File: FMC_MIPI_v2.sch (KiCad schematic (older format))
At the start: 0 parts

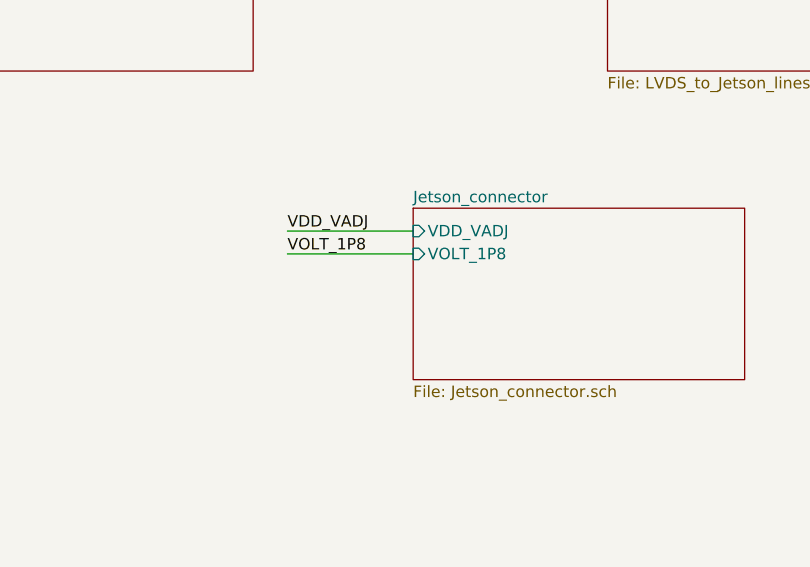
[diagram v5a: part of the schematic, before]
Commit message: added enable line for slow signals
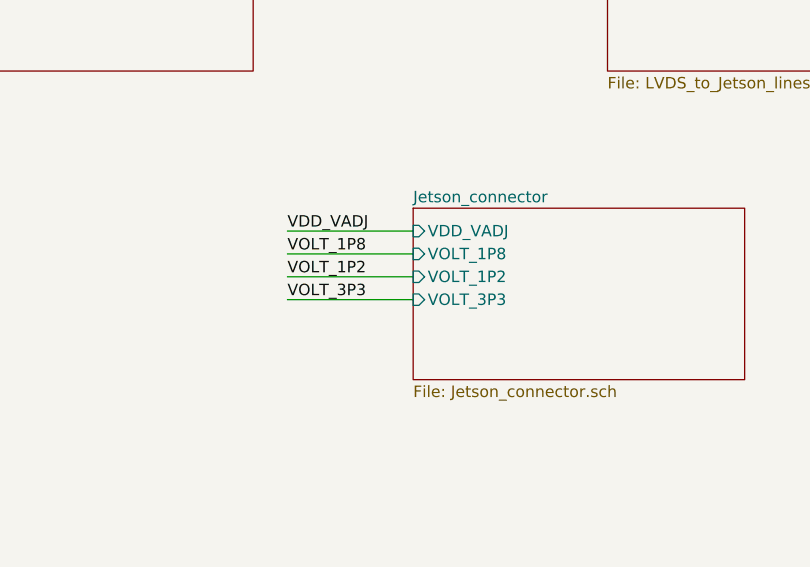
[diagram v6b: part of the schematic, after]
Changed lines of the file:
@@
 F2 "VOLT_1P8" I L 4950 2700 50
 F3 "VDD_VADJ" I L 4950 2600 50
+F4 "VOLT_1P2" I L 4950 2800 50
+F5 "VOLT_3P3" I L 4950 2900 50
 $EndSheet
 Text Notes 7750 5600 0    50   ~ 0
@@
 Wire Notes Line
 	850  6250 850  5500
+Text Label 4400 2800 0    50   ~ 0
+VOLT_1P2
+Wire Wire Line
+	4400 2800 4950 2800
+Text Label 4400 2900 0    50   ~ 0
+VOLT_3P3
+Wire Wire Line
+	4400 2900 4950 2900
 $EndSCHEMATC

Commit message: good, before FMC lines connect
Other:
- note added: "Stackup:\nSingle Ended: 6 mil\nDifferential:\n4 mil Width, 8 mil spacing\n-----\n0.1 mm height to ground plane\n"
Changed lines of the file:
@@
 Wire Wire Line
 	4400 2900 4950 2900
+Text Notes 2300 6100 0    50   ~ 0
+Stackup:\nSingle Ended: 6 mil\nDifferential:\n4  mil Width, 8 mil spacing\n-----\n0.1 mm height to ground plane\n
 $EndSCHEMATC
